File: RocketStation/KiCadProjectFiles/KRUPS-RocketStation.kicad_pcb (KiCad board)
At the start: 4 copper layers, 85 x 56 mm, 54 parts, among them J1 B2P-VH-FB-B, J2 USB_C_Receptacle_USB2.0_16P, J3 RPi5_Header, J4 BM02B-GHS-TBT, J5 BM02B-GHS-TBT, J6 BM02B-GHS-TBT, J7 Conn_02x02, U1 PKU5511ESI, U2 AZ1117-3.3, U3 BME280, U5 SP3232, U6 ESP32-S3-WROOM-2, U7 BNO086, U8 E22-900M33S

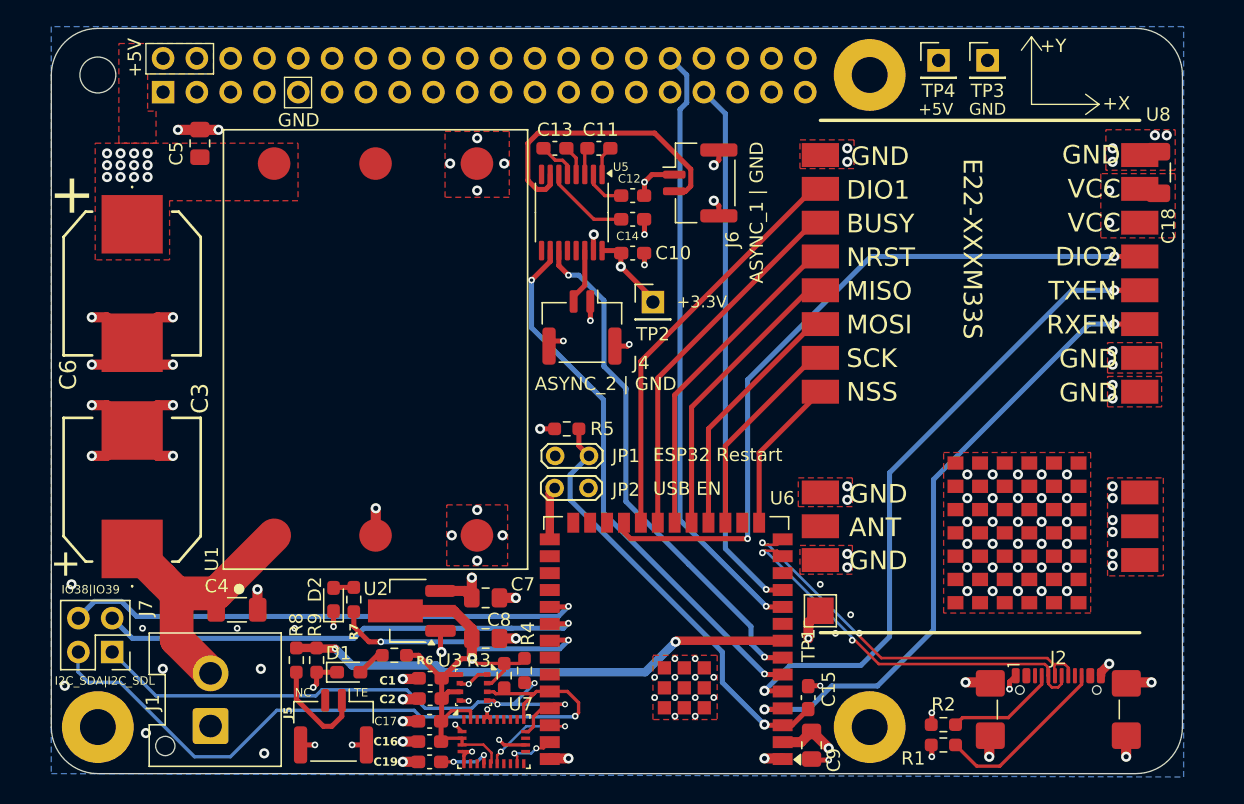
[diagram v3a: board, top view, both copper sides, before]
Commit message: Added fiducials to femtosat (v6) and rocketstation (v4)
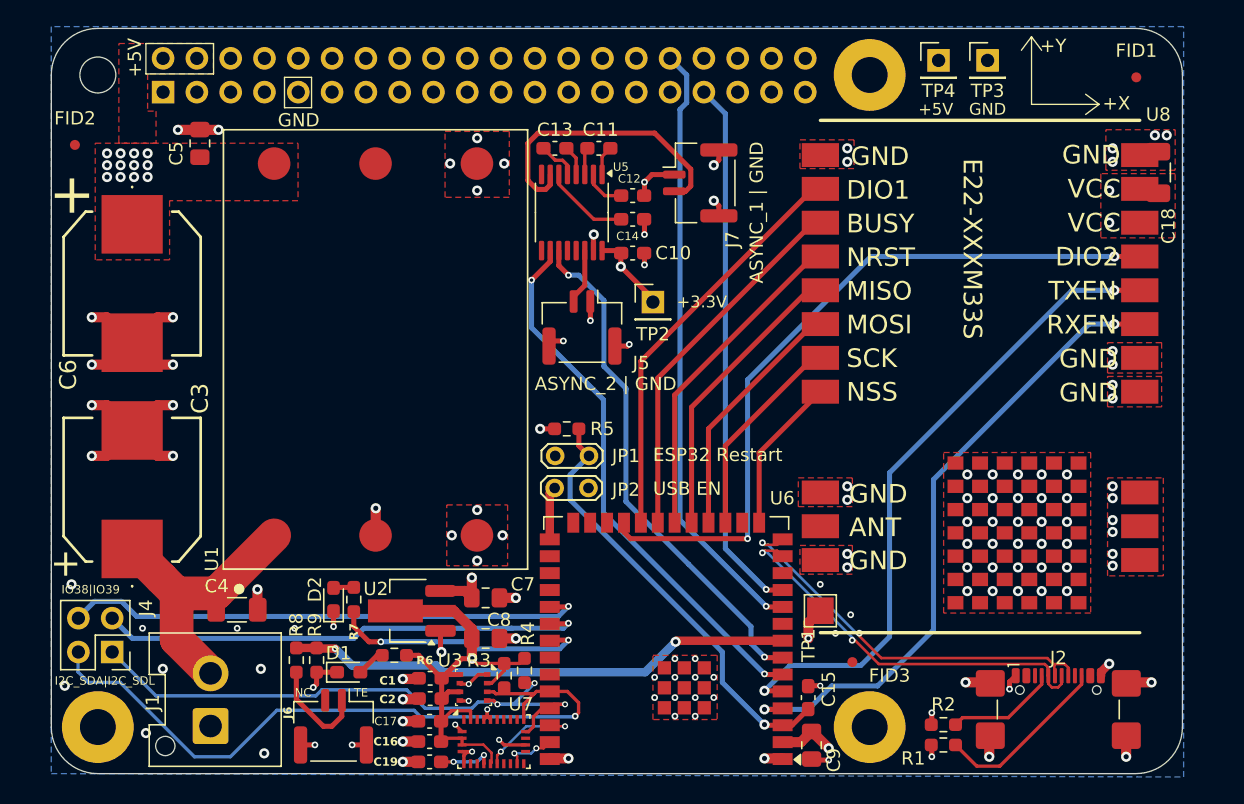
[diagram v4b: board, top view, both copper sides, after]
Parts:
- added FID1: Fiducial, Fiducial:Fiducial_0.75mm_Mask1.5mm, F.Cu at (140.7, 25.8)
- added FID2: Fiducial, Fiducial:Fiducial_0.75mm_Mask1.5mm, F.Cu at (61.0, 30.9)
- added FID3: Fiducial, Fiducial:Fiducial_0.75mm_Mask1.5mm, F.Cu at (119.4, 69.7)
- U6: value ESP32-S3-WROOM-2 -> ESP32-S3-WROOM-1-N16R8
- renumbered J7 to J4, J4 to J5, J5 to J6, J6 to J7
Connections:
- net /IO40 renamed /GPIO_LED
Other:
- board text added: "Space Systems Lab, University of Kentucky, Lexington KY, USA, Earth KRUPS BaseStation/RocketStation Rev: V4 Serial Number: 12-28-2024"
- board text removed: "Space Systems Lab, University of Kentucky, Lexington KY, USA, Earth KRUPS BaseStation/RocketStation Rev: V3 Serial Number: 12-27-2024"

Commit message: Changed to Raspi Pico, 1W radio
- Swapped the ESP32 S3 WROOM to a Raspberry Pi Pico 2 W on both the FemtoSat and RocketStation
- Swapped to 1W LoRa module in place of the 2W EBYTE one
- bunch of layout, documentation, miscellaneous changes
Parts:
- removed C15: 0.1u, Capacitor_SMD:C_0603_1608Metric_Pad1.08x0.95mm_HandSolder
- removed C18: 100u, Capacitor_SMD:C_1206_3216Metric_Pad1.33x1.80mm_HandSolder
- removed C9: 22u, Capacitor_SMD:C_0805_2012Metric_Pad1.18x1.45mm_HandSolder
- removed D2: LED, Diode_SMD:D_0603_1608Metric_Pad1.05x0.95mm_HandSolder
- removed J2: USB_C_Receptacle_USB2.0_16P, Connector_USB:USB_C_Receptacle_GCT_USB4110
- removed J4: Conn_02x02, Connector_PinHeader_2.54mm:PinHeader_2x02_P2.54mm_Vertical
- removed JP1, JP2: Jumper_2_Small_Open, TestPoint:TestPoint_2Pads_Pitch2.54mm_Drill0.8mm
- removed R1, R2: 5.1k, Resistor_SMD:R_0603_1608Metric_Pad0.98x0.95mm_HandSolder
- removed R5: 20k, Resistor_SMD:R_0603_1608Metric_Pad0.98x0.95mm_HandSolder
- removed R7: 68, Resistor_SMD:R_0603_1608Metric_Pad0.98x0.95mm_HandSolder
- removed TP1: TestPoint, TestPoint:TestPoint_Pad_2.0x2.0mm
- removed U8: E22-900M33S, KRUPS-RocketStation:E22-XXXM33S
- added U4: LR62XE, KRUPS-RocketStation:LR62XE, F.Cu at (111.7, 51.1)
- U6: value ESP32-S3-WROOM-1-N16R8 -> Pico_2_W; footprint RF_Module:ESP32-S3-WROOM-2 -> Module:RaspberryPi_Pico_Common_THT
- moved FID1 89.8 mm to (61.7, 68.4)
- moved TP3 53.6 mm to (97.8, 67.7)
- moved U6 51.4 mm to (126.5, 24.9), turned to 0 degrees
- moved TP4 47.5 mm to (106.2, 67.7)
- moved J6 28.0 mm to (99.1, 53.7), turned to 0 degrees
- moved R8 26.6 mm to (101.9, 58.7), turned to 90 degrees
- moved R9 23.8 mm to (100.3, 58.7), turned to -90 degrees
- moved TP2 19.6 mm to (97.8, 61.1)
- moved J7 11.0 mm to (105.9, 44.6), turned to 180 degrees
- moved FID3 8.08 mm to (113.8, 75.6)
- moved J5 0.13 mm to (99.0, 44.6)
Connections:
- J3 pad 10: unconnected-(J3-GPIO15/RXD-Pad10) -> /RPI_UART_RX
- J3 pad 32: /RPI_UART4_TX -> unconnected-(J3-PWM0/GPIO12-Pad32)
- J3 pad 33: /RPI_UART4_RX -> unconnected-(J3-PWM1/GPIO13-Pad33)
- J3 pad 8: unconnected-(J3-GPIO14/TXD-Pad8) -> /RPI_UART_TX
- U6 pad 1: GND -> /RPI_UART_RX
- U6 pad 10: /RPI_UART4_TX -> /SPI_MOSI
- U6 pad 11: /RPI_UART4_RX -> /SPI_MISO
- U6 pad 12: unconnected-(U6-IO8-Pad12) -> /SPI_NSS
- U6 pad 13: /USB_D- -> GND
- U6 pad 14: /USB_D+ -> /LORA_DIO1
- U6 pad 15: /SPI_NSS -> /LORA_BUSY
- U6 pad 16: unconnected-(U6-IO46-Pad16) -> /~{LORA_RESET}
- U6 pad 17: /SPI_CLK -> /LORA_ANTSW
- U6 pad 18: /SPI_MOSI -> GND
- U6 pad 19: /SPI_MISO -> /I2C_SDA
- U6 pad 2: +3V3 -> /RPI_UART_TX
- U6 pad 20: /~{LORA_RESET} -> /I2C_SCL
- U6 pad 21: /LORA_BUSY -> unconnected-(U6-GPIO16-Pad21)
- U6 pad 22: /LORA_DIO1 -> unconnected-(U6-GPIO17-Pad22)
- U6 pad 23: /LORA_DIO2 -> GND
- U6 pad 25: unconnected-(U6-IO48-Pad25) -> /BNO086_HINTN
- U6 pad 26: unconnected-(U6-IO45-Pad26) -> /~{BNO086_RESET}
- U6 pad 27: /USB_EN -> unconnected-(U6-GPIO21-Pad27)
- U6 pad 28: unconnected-(U6-NC-Pad28) -> GND
- U6 pad 3: /ESP32_EN -> GND
- U6 pad 31: /IO38 -> /TE_SENSE
- U6 pad 32: /IO39 -> unconnected-(U6-GPIO27_ADC1-Pad32)
- U6 pad 33: /GPIO_LED -> GND
- U6 pad 36: /I2C_SDA -> unconnected-(U6-3V3-Pad36)
- U6 pad 37: /I2C_SCL -> unconnected-(U6-3V3_EN-Pad37)
- U6 pad 38: /~{BNO086_RESET} -> GND
- U6 pad 39: /BNO086_HINTN -> +5V
- U6 pad 4: /LORA_RXEN -> unconnected-(U6-GPIO2-Pad4)
- U6 pad 40: GND -> unconnected-(U6-VBUS-Pad40)
- U6 pad 5: /LORA_TXEN -> unconnected-(U6-GPIO3-Pad5)
- U6 pad 8: /TE_SENSE -> GND
- U6 pad 9: unconnected-(U6-IO16-Pad9) -> /SPI_CLK
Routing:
- net /RPI_UART_RX: track 0.00 -> 55.8 mm
- net /LORA_DIO2: track 55.5 -> 0.00 mm, vias 2 -> 0
- net /RPI_UART_TX: track 0.00 -> 55.4 mm
- net /BNO086_HINTN: track 3.88 -> 56.8 mm, vias 2 -> 1
- net /~{BNO086_RESET}: track 7.82 -> 58.9 mm, vias 2 -> 1
- net /LORA_TXEN: track 49.3 -> 0.00 mm, vias 2 -> 0
- net /LORA_RXEN: track 48.2 -> 0.00 mm, vias 2 -> 0
- net /LORA_ANTSW: track 0.00 -> 46.6 mm
- net /RPI_UART4_TX: track 45.8 -> 0.00 mm, vias 1 -> 0
- net /RPI_UART4_RX: track 40.6 -> 0.00 mm, vias 1 -> 0
- net /IO38: track 39.6 -> 0.00 mm, vias 1 -> 0
- net /IO39: track 36.8 -> 0.00 mm, vias 1 -> 0
- net /ESP32_EN: track 33.0 -> 0.00 mm, vias 1 -> 0
- net +3V3: track 124.3 -> 92.6 mm, vias 5 -> 3
- net /USB_D+: track 30.3 -> 0.00 mm, vias 2 -> 0
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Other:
- board size 85 x 56 mm -> 87.6 x 56 mm
- board text added: "Space Systems Lab, University of Kentucky, Lexington KY, USA, Earth KRUPS BaseStation/RocketStation Rev: V5 Serial Number: 02-09-2025"
- board text removed: "ESP32 Restart"
- board text removed: "I2C_SDA|I2C_SDL"
- board text removed: "IO38|IO39"
- board text removed: "PCB Antenna"
- board text removed: "Space Systems Lab, University of Kentucky, Lexington KY, USA, Earth KRUPS BaseStation/RocketStation Rev: V4 Serial Number: 12-28-2024"
- board text removed: "USB EN"

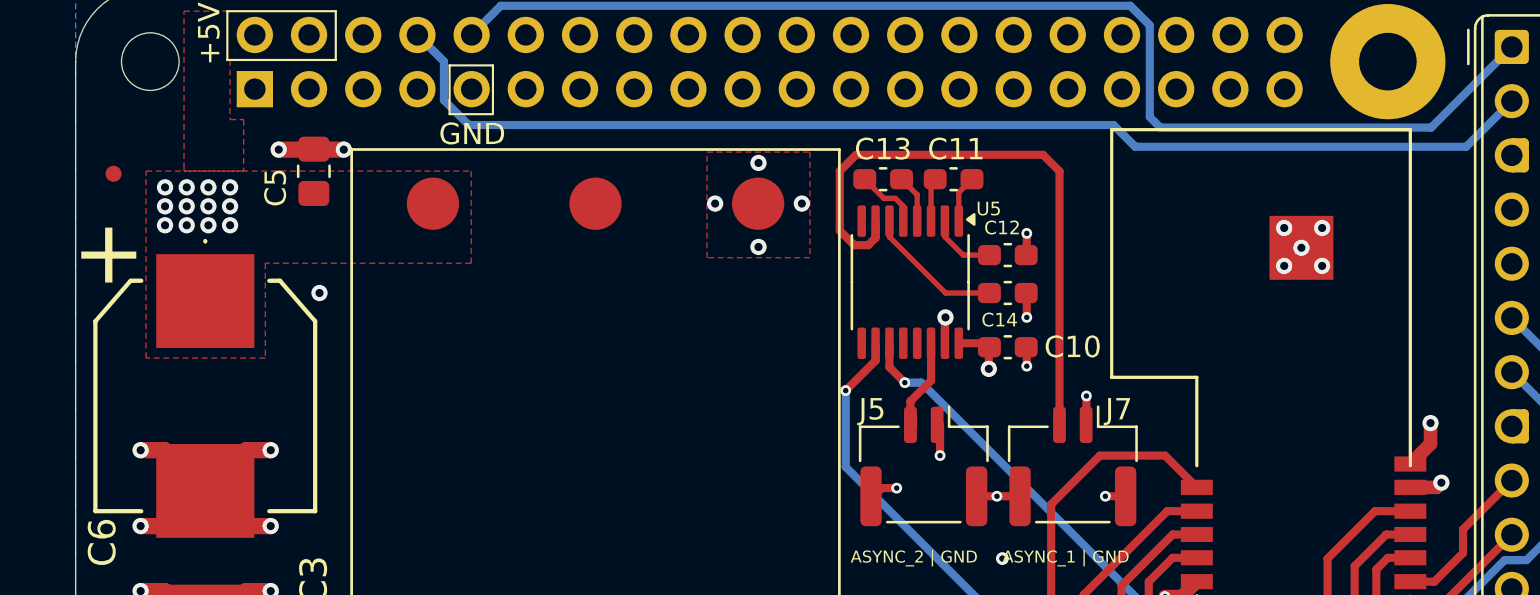
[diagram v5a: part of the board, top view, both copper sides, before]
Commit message: Removed LR62XE adapter, corrected readme, fixed silkscreen on LR62XE footprint
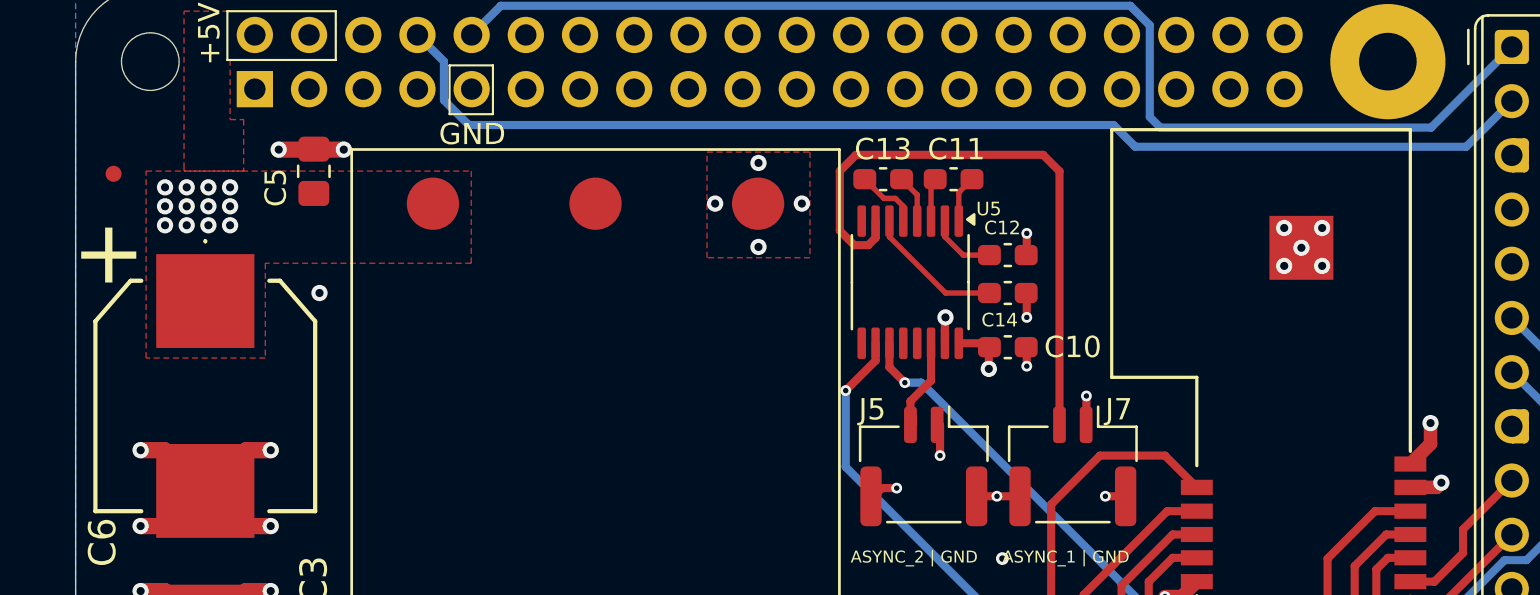
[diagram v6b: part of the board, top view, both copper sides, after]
